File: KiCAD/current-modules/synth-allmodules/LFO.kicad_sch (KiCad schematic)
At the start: 0 parts

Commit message: Started LFO
Additions:
- Some LFO components
Changes:
- None
Removals:
- None
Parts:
- added U12: TL074, symbol Amplifier_Operational:TL074

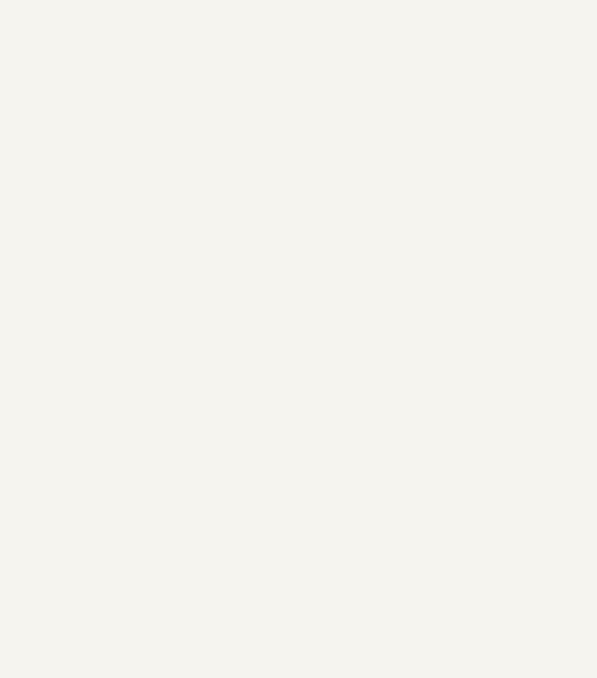
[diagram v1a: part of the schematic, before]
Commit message: More LFO Components
Additions:
- Some LFO components
Changes:
- None
Removals:
- None
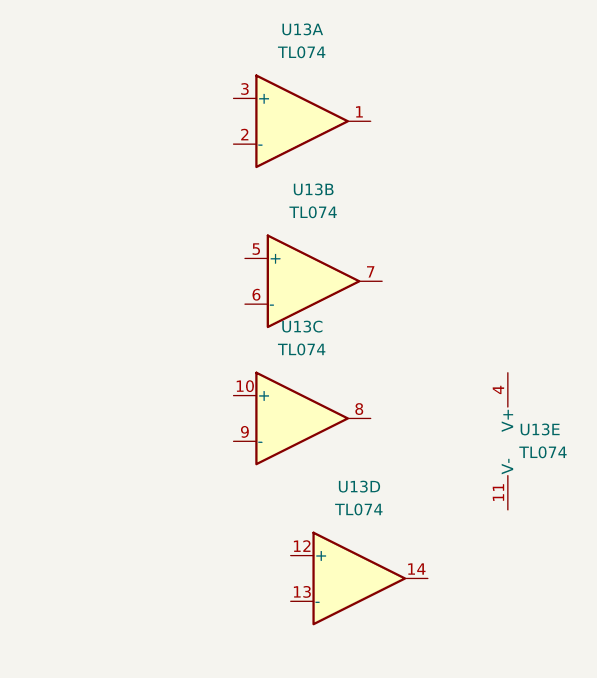
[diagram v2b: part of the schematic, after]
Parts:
- added U13: TL074, symbol Amplifier_Operational:TL074

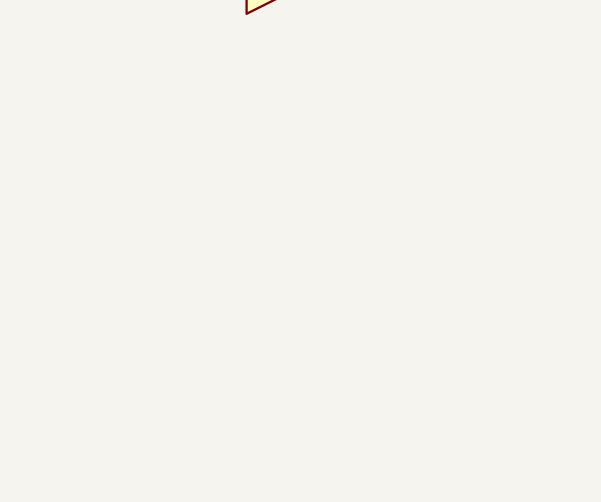
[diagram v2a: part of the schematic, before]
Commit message: More LFO Components
Additions:
- Some LFO components
Changes:
- None
Removals:
- None
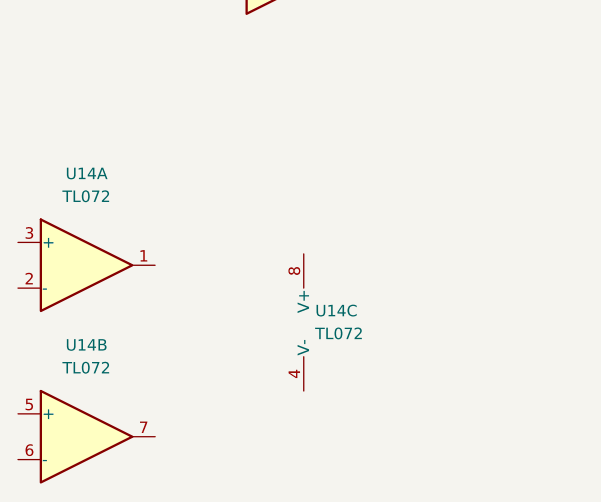
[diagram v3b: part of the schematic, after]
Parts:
- added U14: TL072, symbol Amplifier_Operational:TL072

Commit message: Added Remaining LFO Components
Additions:
- Remaining LFO components
Changes:
- None
Removals:
- None
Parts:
- added C40: C, symbol Device:C
- added C41: C_Polarized, symbol Device:C_Polarized
- added D31: 1N4148, Diode_THT:D_DO-35_SOD27_P7.62mm_Horizontal, symbol Diode:1N4148
- added D32: LED, symbol Device:LED
- added Q10: BC547, Package_TO_SOT_THT:TO-92_Inline, symbol Transistor_BJT:BC547
- added R68: R, symbol Device:R
- added RV31: R_Potentiometer, symbol Device:R_Potentiometer
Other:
- moved on the sheet: U12C, U12D, U13C, U13D

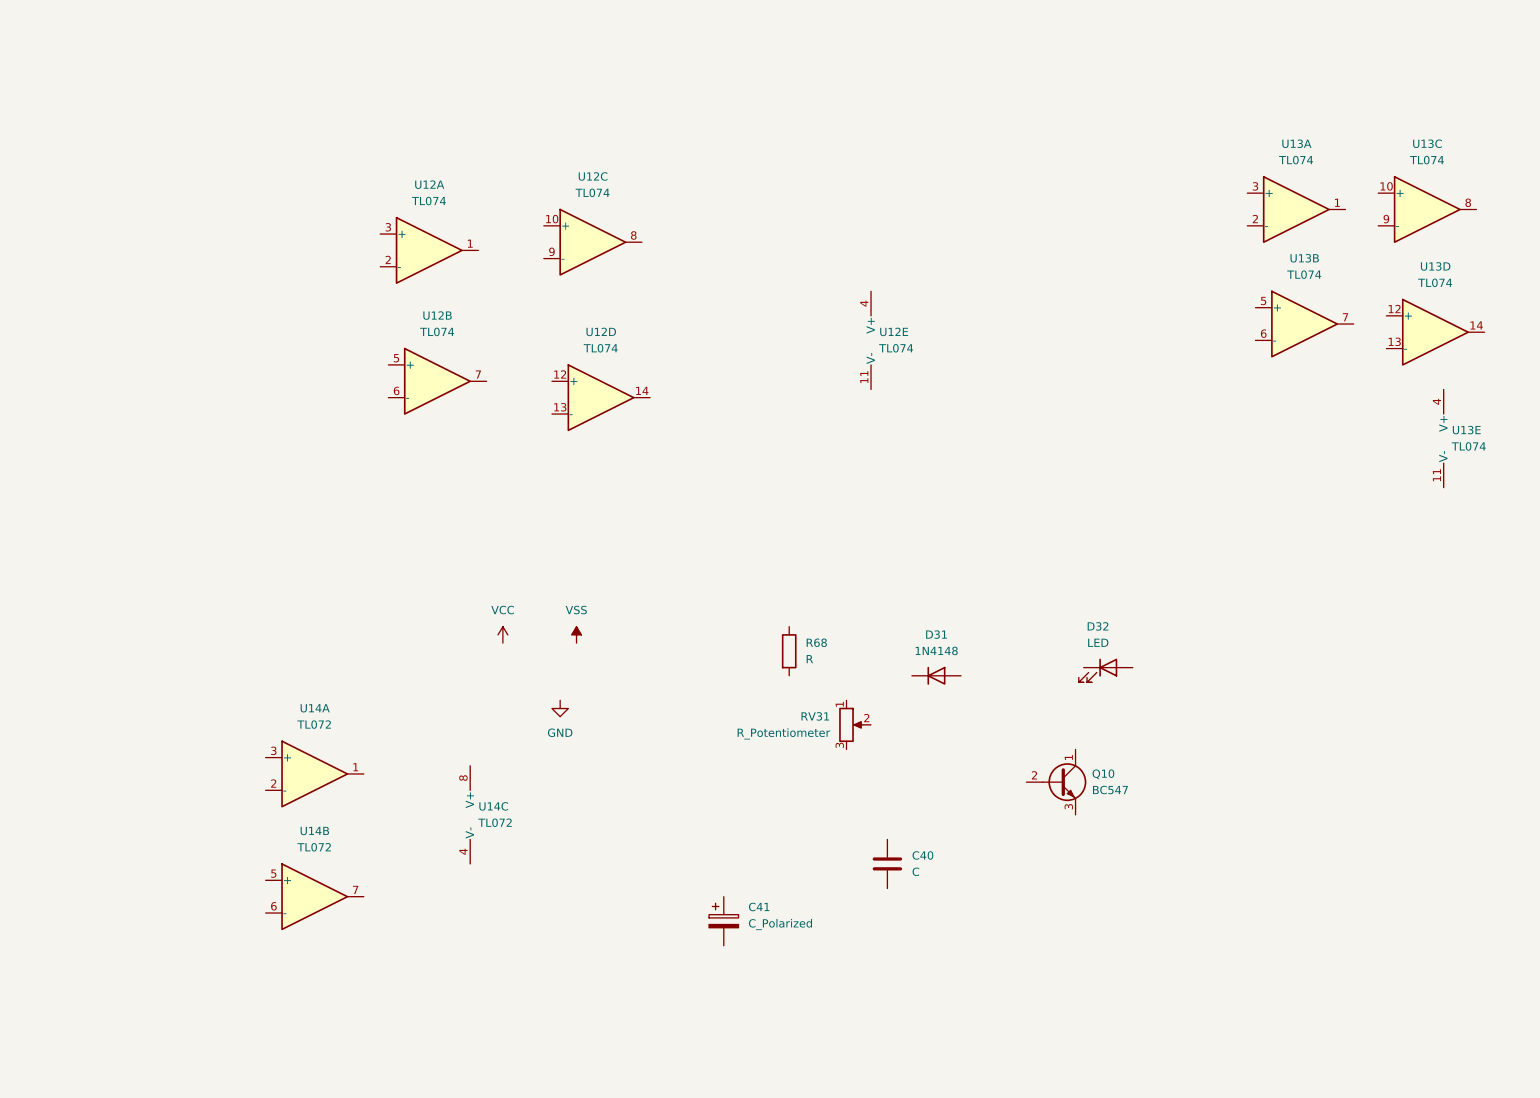
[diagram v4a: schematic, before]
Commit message: Initial Component Placement
Additions:
- None
Changes:
- Vague component placement for one of the LFOs. No values on components yet.
Removals:
- None
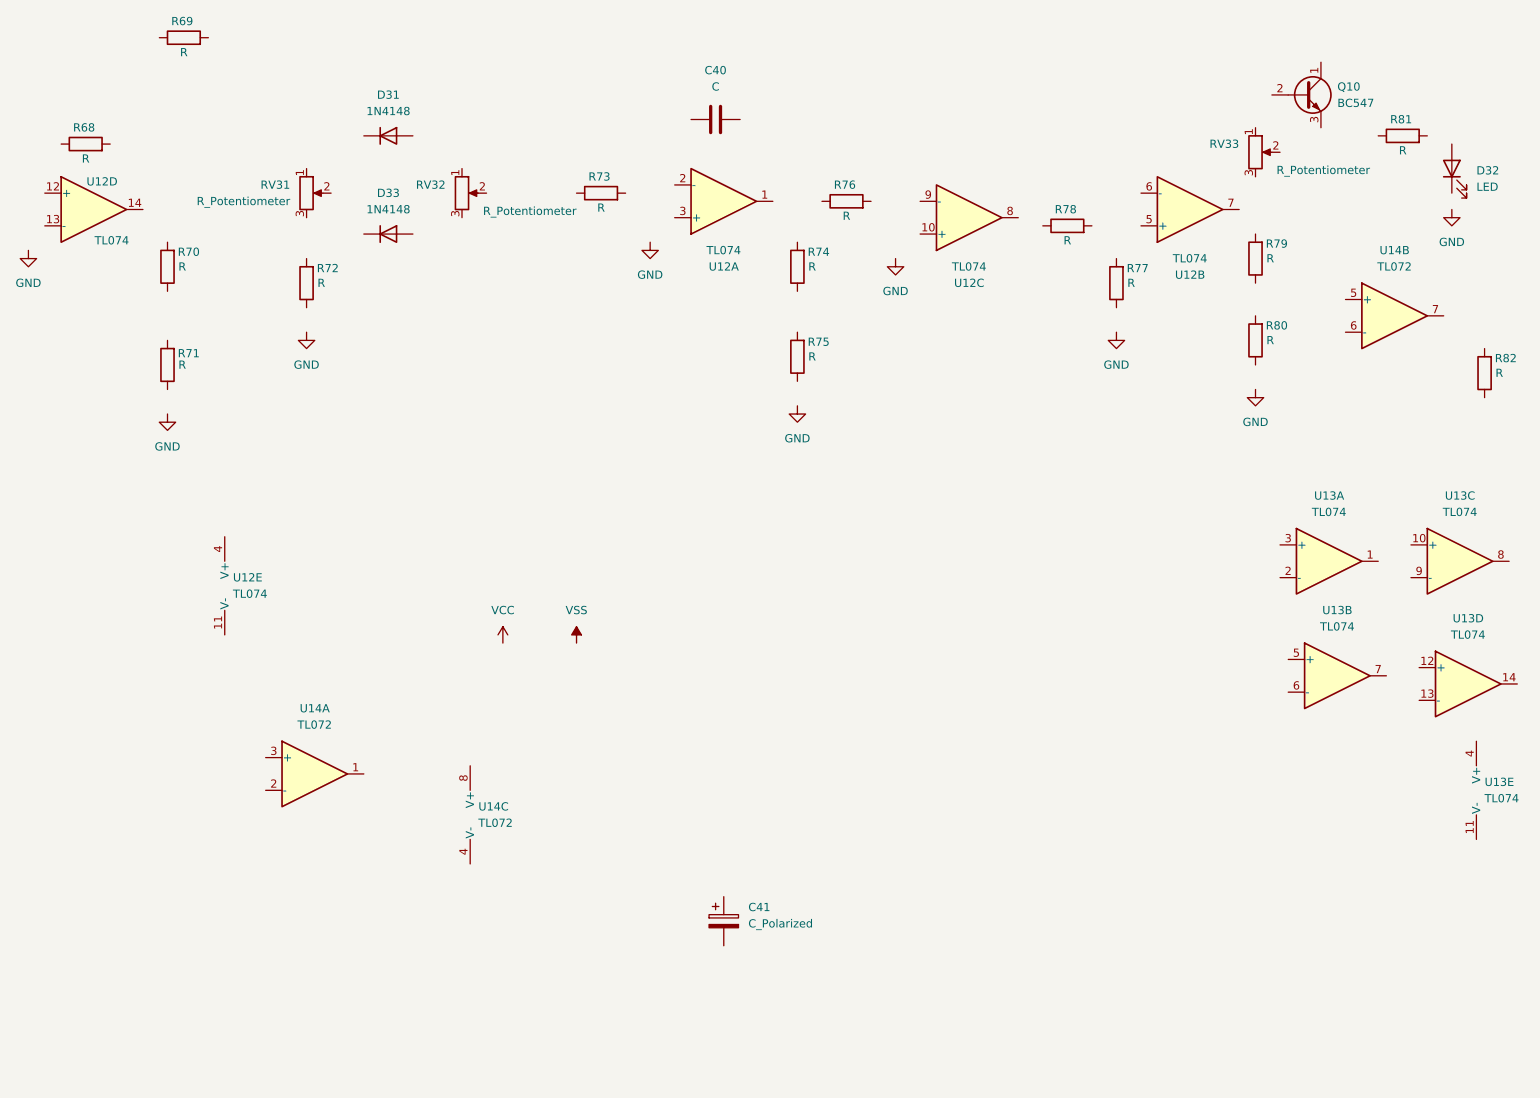
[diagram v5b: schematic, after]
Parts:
- added D33: 1N4148, Diode_THT:D_DO-35_SOD27_P7.62mm_Horizontal, symbol Diode:1N4148
- added R69, R70, R71, R72, R73, R74, R75, R76, R77, R78, R79, R80, R81, R82: R, symbol Device:R
- added RV32, RV33: R_Potentiometer, symbol Device:R_Potentiometer
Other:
- moved on the sheet: C40, D31, D32, Q10, R68, RV31, U12A, U12B, U12C, U12D, U12E, U13A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

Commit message: Half Component Values
Additions:
- Half of the components' values have been assigned
Changes:
- None
Removals:
- None
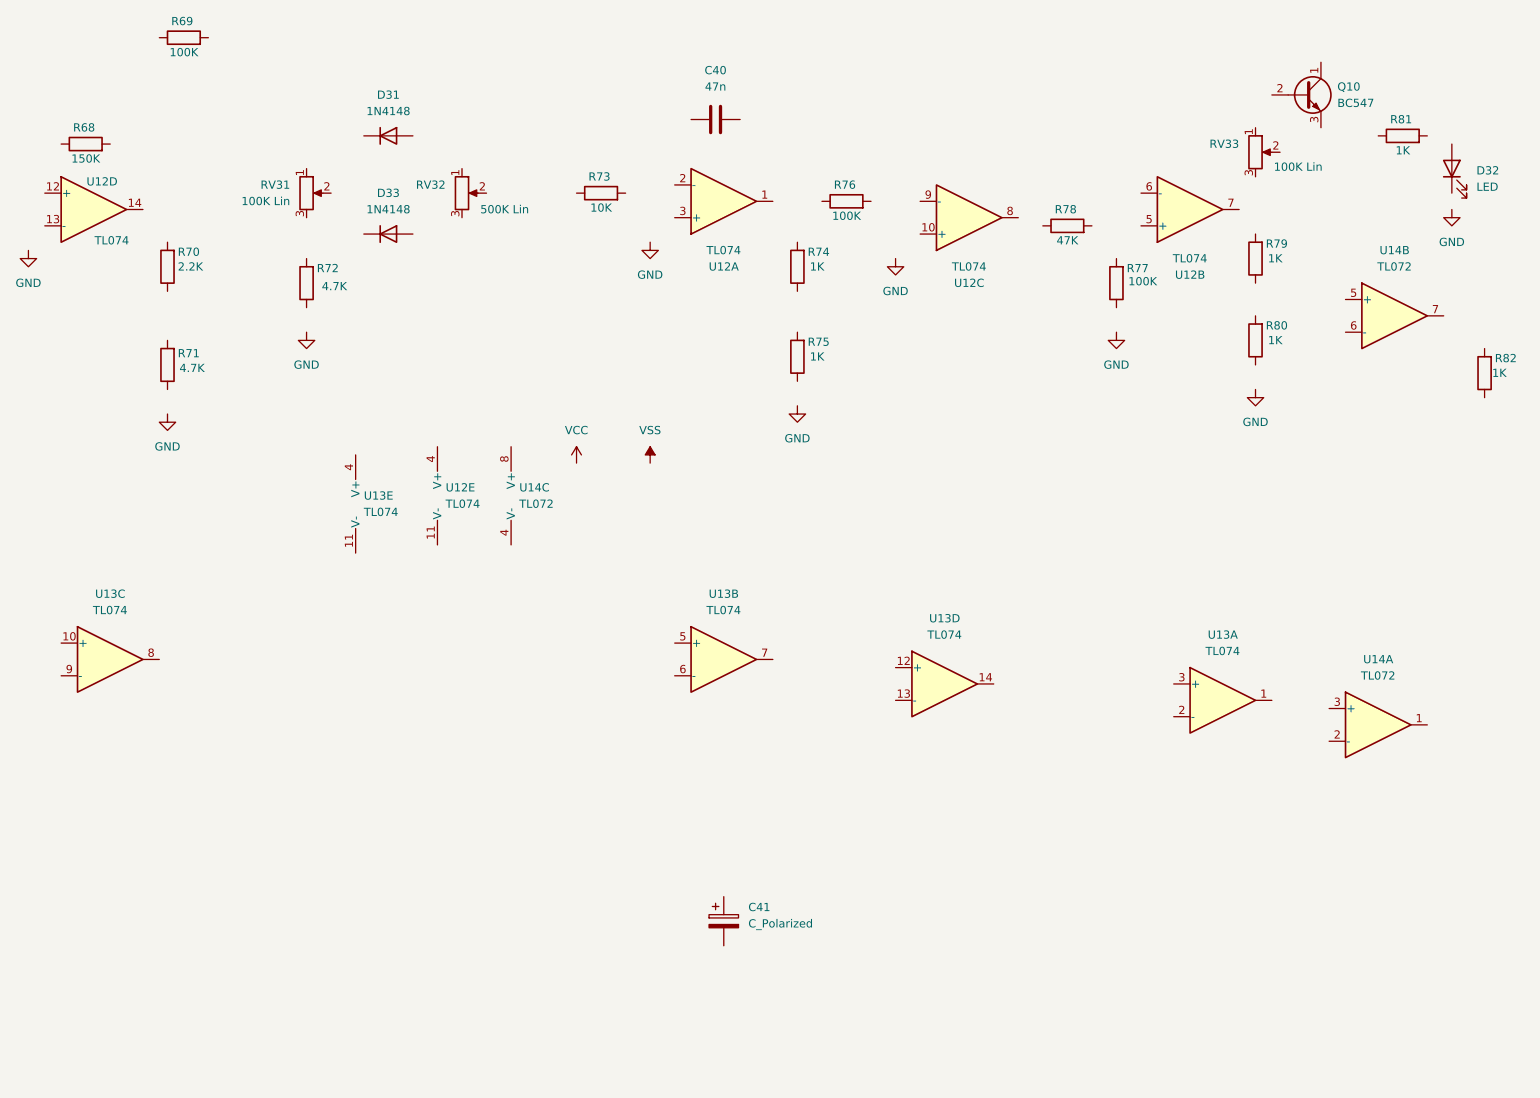
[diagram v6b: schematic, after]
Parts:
- C40: value C -> 47n
- R68: value R -> 150K
- R69, R76, R77: value R -> 100K
- R70: value R -> 2.2K
- R71, R72: value R -> 4.7K
- R73: value R -> 10K
- R74, R75, R79, R80, R81, R82: value R -> 1K
- R78: value R -> 47K
- RV31, RV33: value R_Potentiometer -> 100K Lin
- RV32: value R_Potentiometer -> 500K Lin
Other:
- moved on the sheet: U12E, U13A, U13B, U13C, U13D, U13E, U14A, U14C

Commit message: Other Half Placed
Additions:
- Second LFO module components placed and assigned values.
- Decoupling caps
Changes:
- None
Removals:
- None
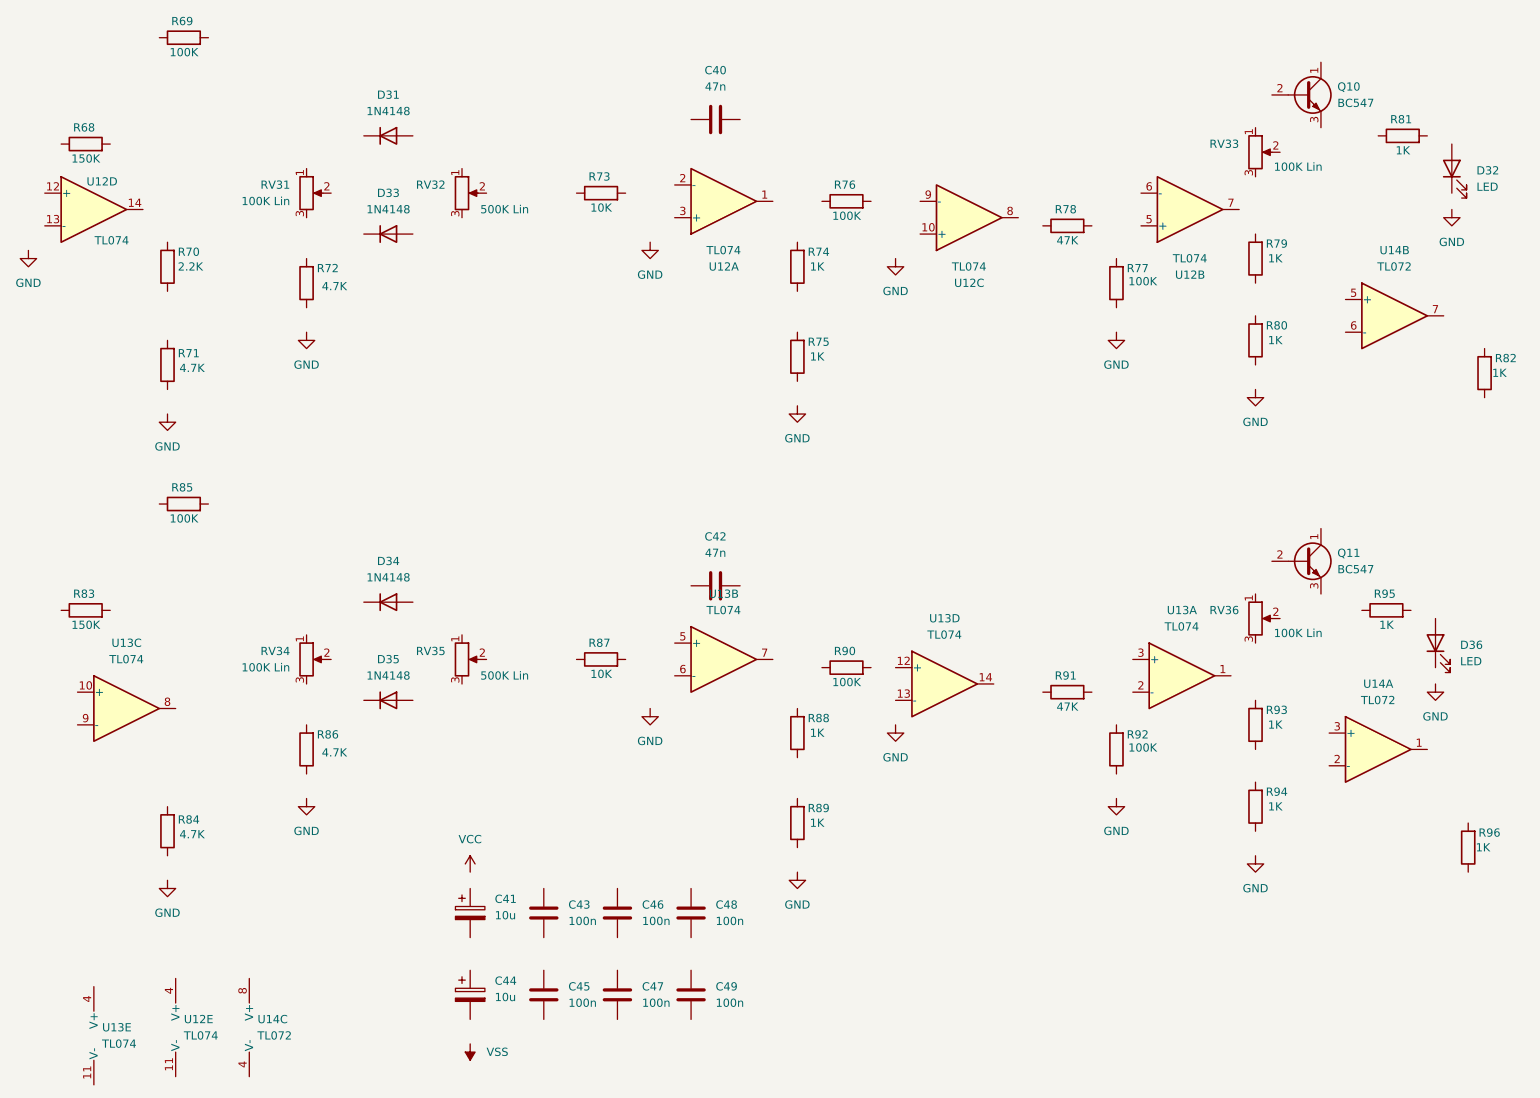
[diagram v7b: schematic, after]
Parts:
- added C42: 47n, symbol Device:C
- added C43, C45, C46, C47, C48, C49: 100n, symbol Device:C
- added C44: 10u, symbol Device:C_Polarized
- added D34, D35: 1N4148, Diode_THT:D_DO-35_SOD27_P7.62mm_Horizontal, symbol Diode:1N4148
- added D36: LED, symbol Device:LED
- added Q11: BC547, Package_TO_SOT_THT:TO-92_Inline, symbol Transistor_BJT:BC547
- added R83: 150K, symbol Device:R
- added R84, R86: 4.7K, symbol Device:R
- added R85, R90, R92: 100K, symbol Device:R
- added R87: 10K, symbol Device:R
- added R88, R89, R93, R94, R95, R96: 1K, symbol Device:R
- added R91: 47K, symbol Device:R
- added RV34, RV36: 100K Lin, symbol Device:R_Potentiometer
- added RV35: 500K Lin, symbol Device:R_Potentiometer
- C41: value C_Polarized -> 10u
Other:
- moved on the sheet: C41, U12E, U13A, U13C, U13E, U14A, U14C

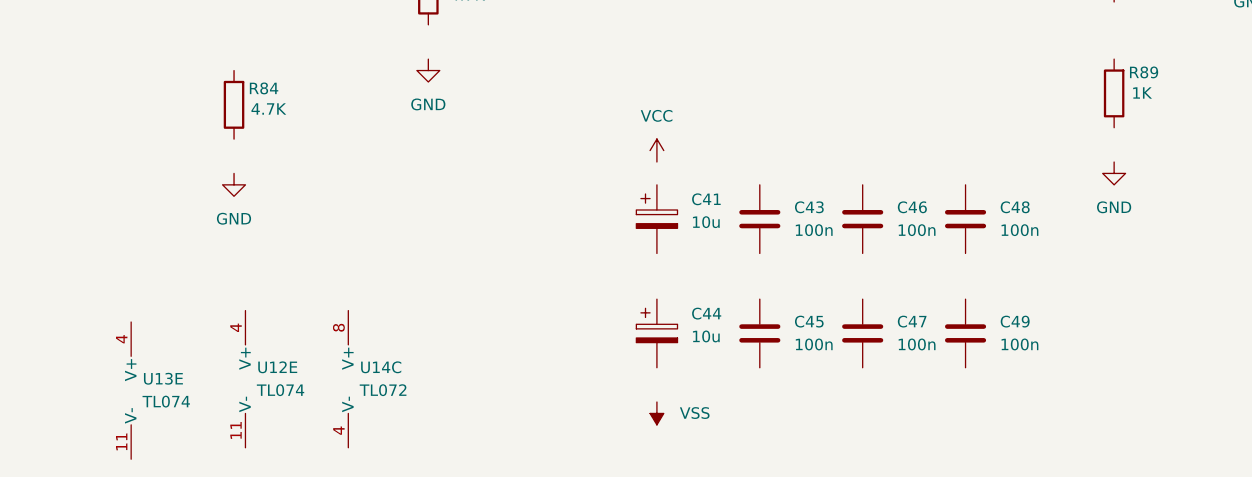
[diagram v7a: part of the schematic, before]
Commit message: Power Connected
Additions:
-  None
Changes:
- uC power pins connected
- Decoupling caps connected
Removals:
- None
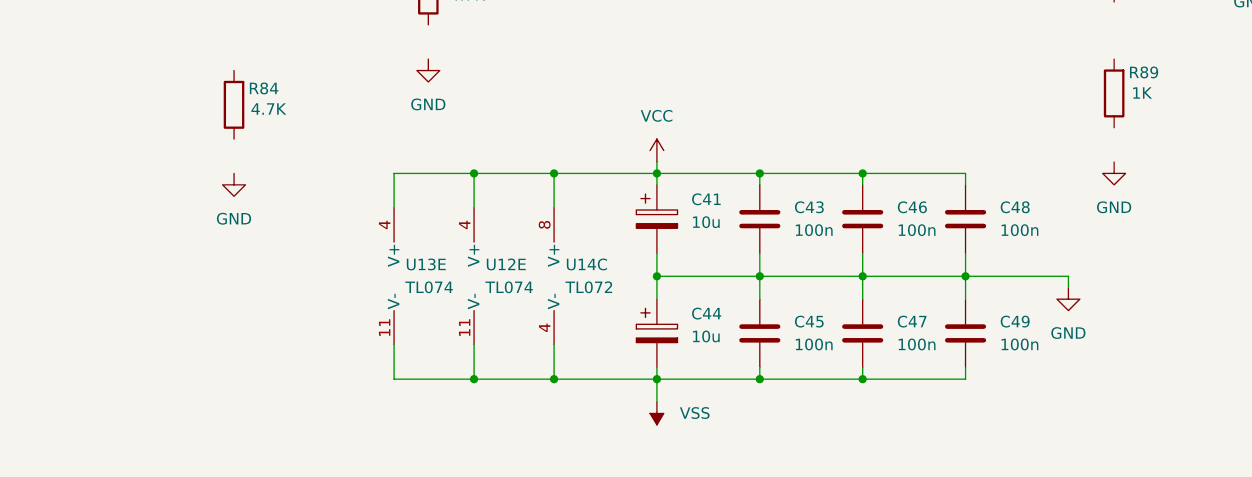
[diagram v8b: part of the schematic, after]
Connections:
- net GND: now also C41.2, C43.1, C44.1, C45.2, C46.1, C47.2, C48.1, C49.2
- net VCC: now also C41.1, C43.2, C46.2, C48.2, U12.4 (V+), U13.4 (V+), U14.8 (V+)
- net VSS: now also C44.2, C45.1, C47.1, C49.1, U12.11 (V-), U13.11 (V-), U14.4 (V-)
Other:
- moved on the sheet: U12E, U13E, U14C
